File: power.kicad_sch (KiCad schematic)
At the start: 16 parts, among them U1 HT7533-1, U2 TLV62569DBV

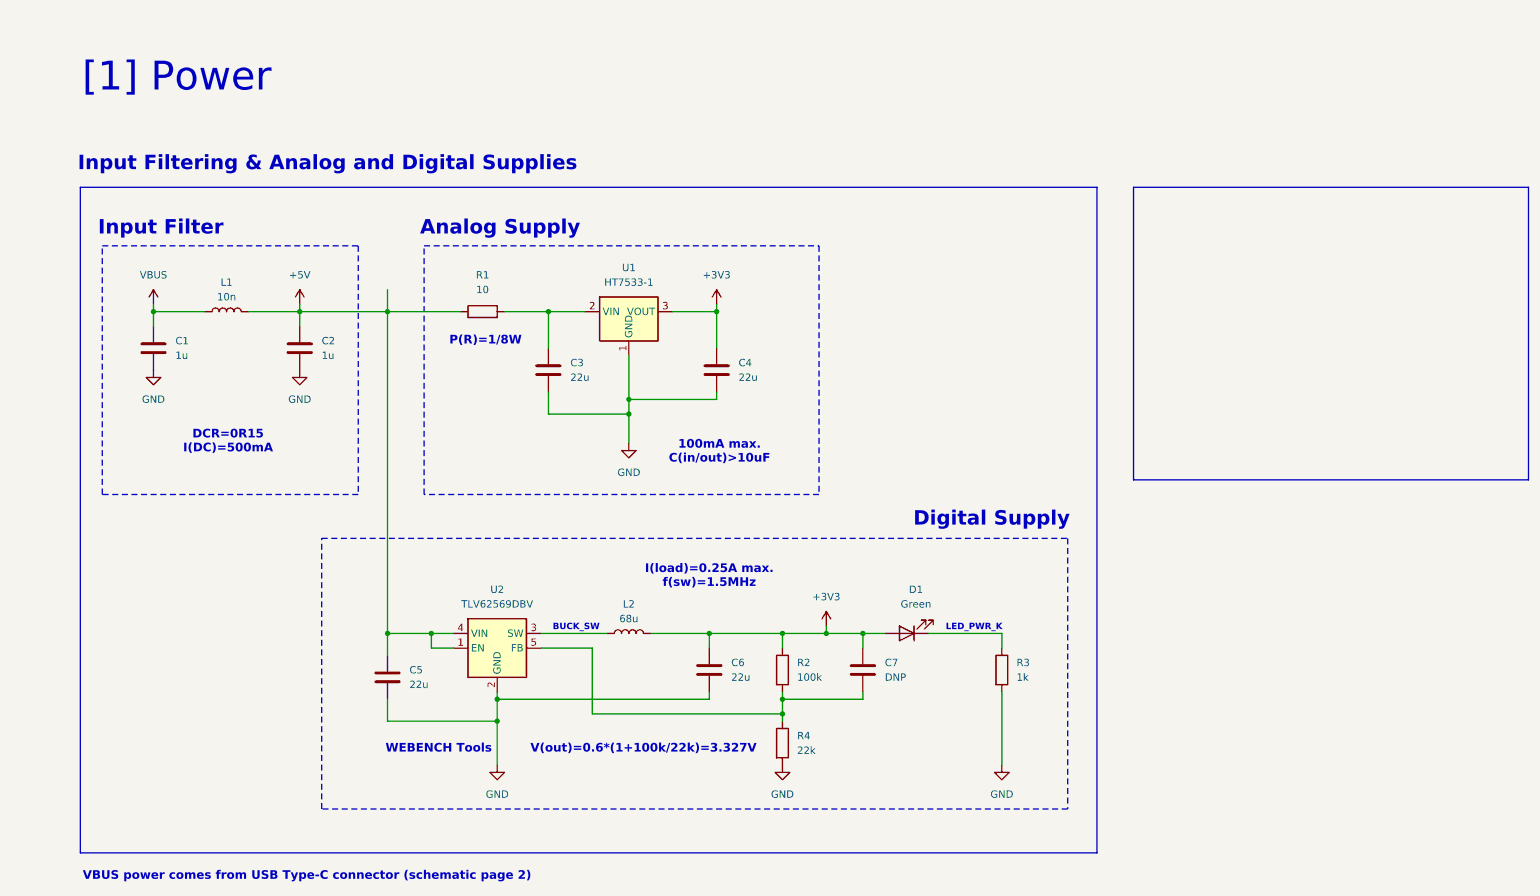
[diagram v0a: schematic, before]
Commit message: Added notes for 3rd lesson: Power Supply Design
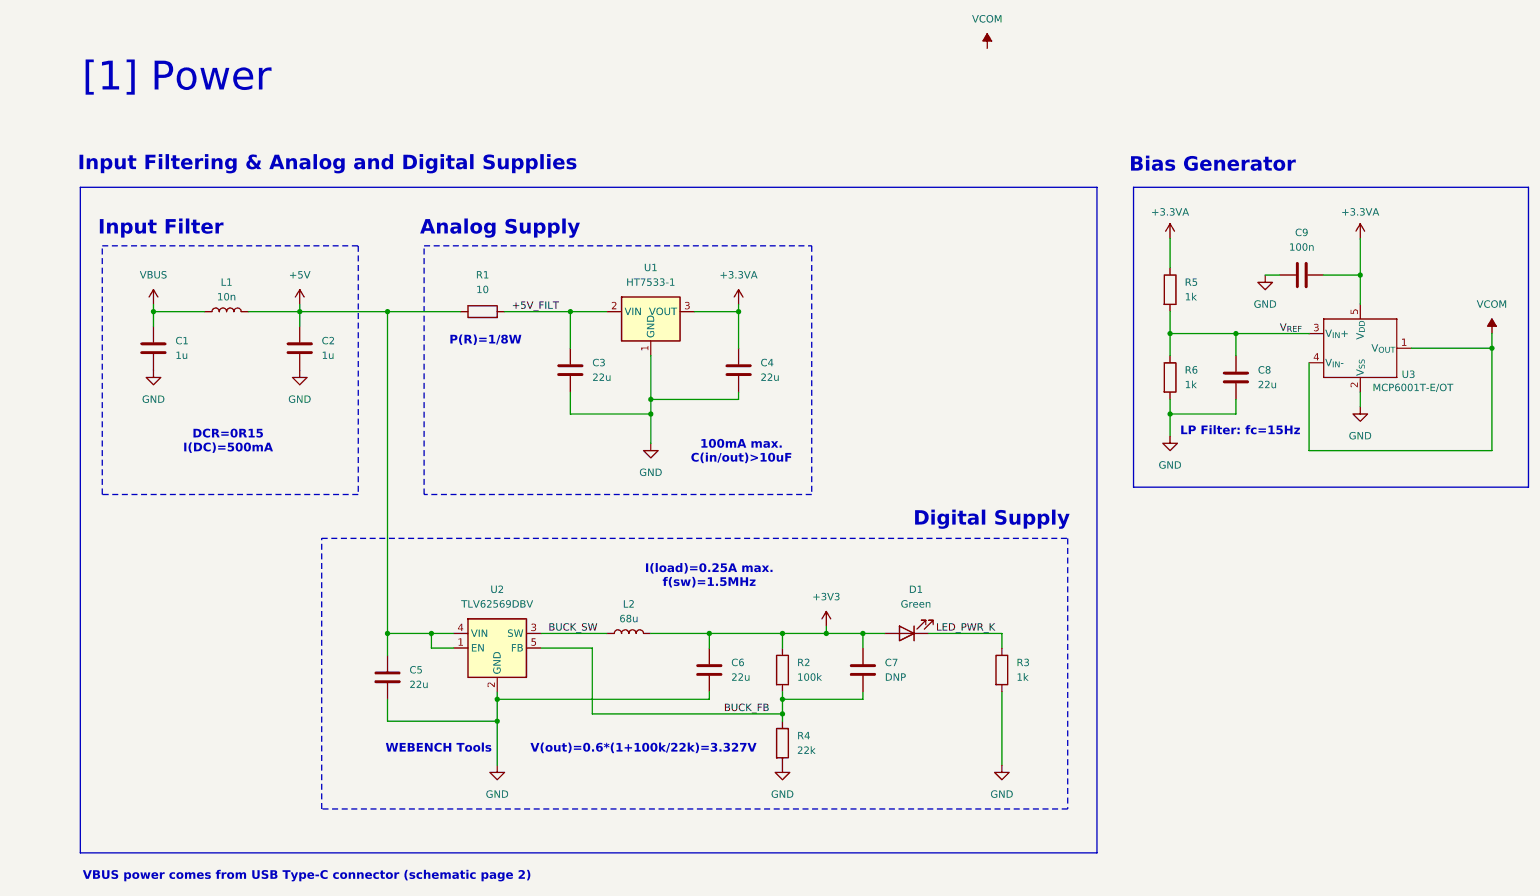
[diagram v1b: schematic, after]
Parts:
- added C8: 22u, symbol Device:C
- added C9: 100n, symbol Device:C
- added R5, R6: 1k, symbol Device:R
- added U3: MCP6001T-E/OT, SOT-23-5_MC_MCH, symbol bias_generator_ic:MCP6001T-E_OT
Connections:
- net +3V3: no longer C4.1, U1.3 (VOUT)
- net GND: now also C8.2, C9.1, R6.2, U3.2 (V_{SS})
- net +5V_FILT: now reaches C3.1, R1.2, U1.2 (VIN)
- net BUCK_SW: now reaches L2.1, U2.3 (SW)
- net BUCK_FB: now reaches C7.2, R2.2, R4.1, U2.5 (FB)
- net LED_PWR_K: now reaches D1.1 (K), R3.1
- new net +3.3VA: C4.1, C9.2, R5.1, U1.3 (VOUT), U3.5 (V_{DD})
- new net VCOM: U3.1 (V_{OUT}), U3.4 (V_{IN}-)
- new net V_{REF}: C8.1, R5.2, R6.1, U3.3 (V_{IN}+)
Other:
- note added: "Bias Generator"
- note added: "LP Filter: fc=15Hz"
- note removed: "BUCK_SW"
- note removed: "LED_PWR_K"
- moved on the sheet: C3, C4, U1
